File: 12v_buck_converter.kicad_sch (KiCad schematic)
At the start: 23 parts, among them IC1 TPS56A37RPAR, Q4 BUK9K52-60RAX

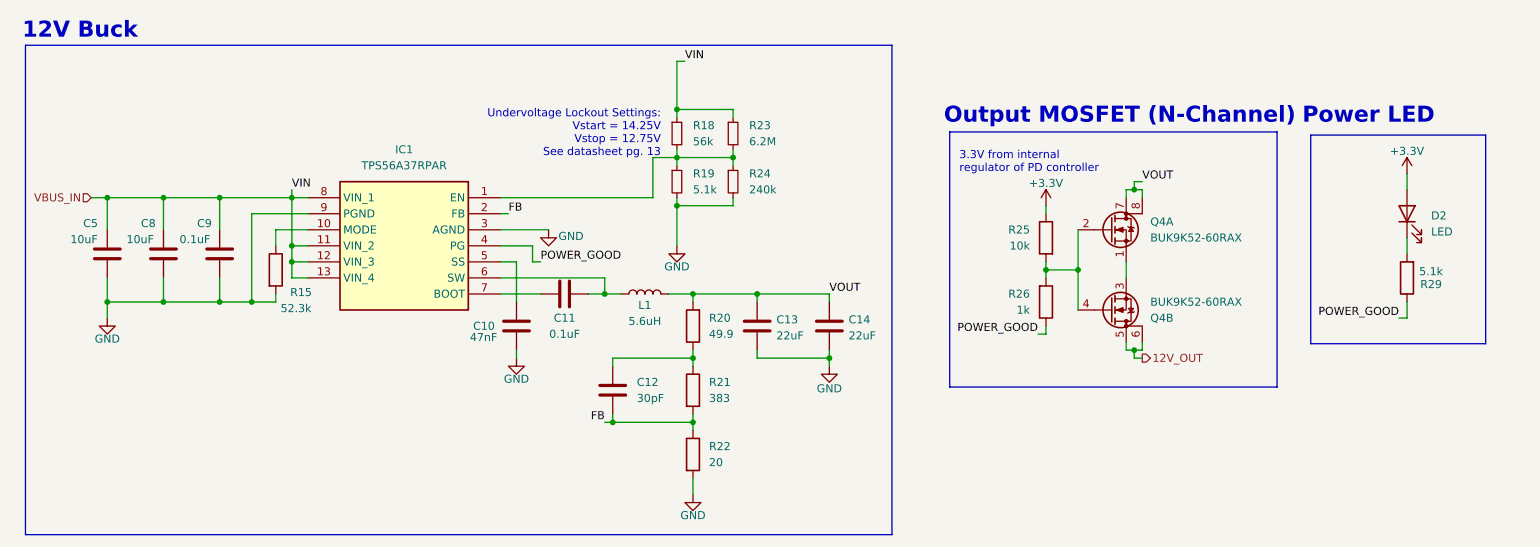
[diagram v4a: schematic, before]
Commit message: updated with some new footprints (have yet to finish footprint assignment; also need to switch out inductor for 5V buck)
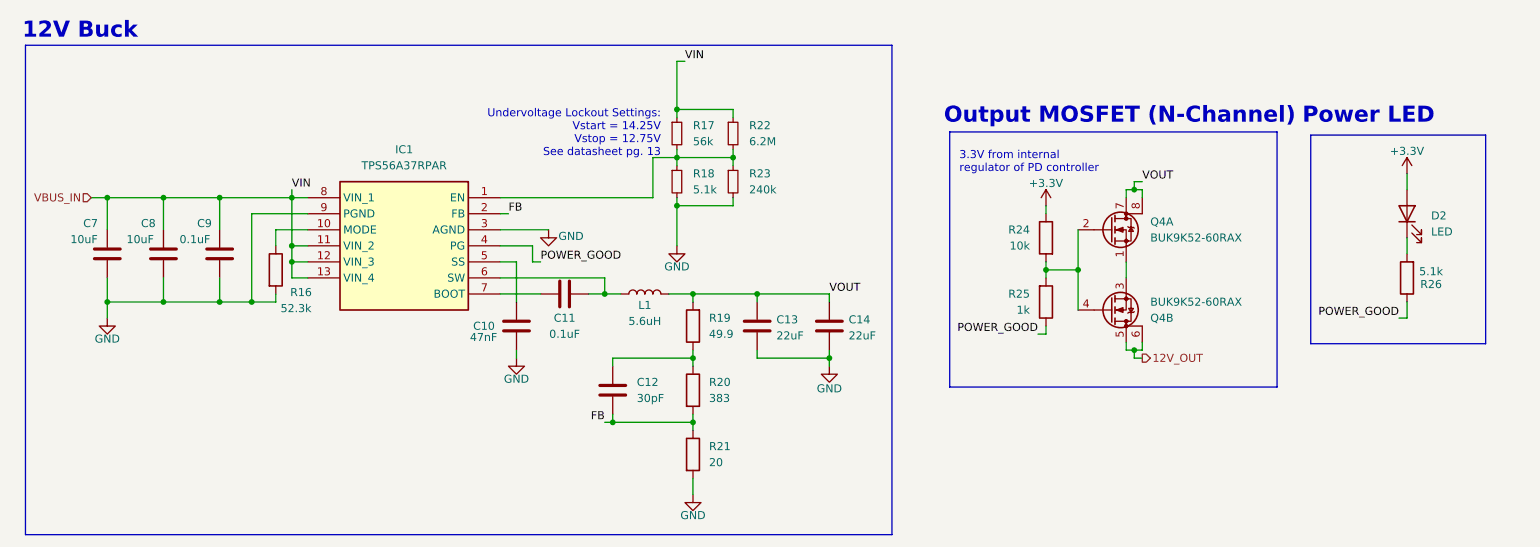
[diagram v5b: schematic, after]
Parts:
- C10, C11, C12, C13, C14, C8, C9: footprint (none) -> Capacitor_SMD:C_0805_2012Metric
- C7: renamed from C5; footprint (none) -> Capacitor_SMD:C_0805_2012Metric
- IC1: footprint TPS56A37RPAR -> UTSVT_Power:TPS56A37RPAR
- L1: footprint (none) -> UTSVT_Passive:INDPM135125X640N; Mouser Part Number (none) -> SRP1265A-5R6M
- R16: renamed from R15; footprint (none) -> Resistor_SMD:R_0805_2012Metric
- R17: renamed from R18; footprint (none) -> Resistor_SMD:R_0805_2012Metric
- R18: renamed from R19; footprint (none) -> Resistor_SMD:R_0805_2012Metric
- R19: renamed from R20; footprint (none) -> Resistor_SMD:R_0805_2012Metric
- R20: renamed from R21; footprint (none) -> Resistor_SMD:R_0805_2012Metric
- R21: renamed from R22; footprint (none) -> Resistor_SMD:R_0805_2012Metric
- R22: renamed from R23; footprint (none) -> Resistor_SMD:R_0805_2012Metric
- R23: renamed from R24; footprint (none) -> Resistor_SMD:R_0805_2012Metric
- R24: renamed from R25; footprint (none) -> Resistor_SMD:R_0805_2012Metric
- R25: renamed from R26; footprint (none) -> Resistor_SMD:R_0805_2012Metric
- R26: renamed from R29; footprint (none) -> Resistor_SMD:R_0805_2012Metric
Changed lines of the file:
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@@
 			)
 		)
-		(property "Footprint" ""
+		(property "Footprint" "Capacitor_SMD:C_0805_2012Metric"
 			(at 54.3052 99.06 0)
 			(effects
@@
 		(on_board yes)
 		(dnp no)
-		(property "Reference" "C5"
+		(property "Reference" "C7"
 			(at 40.64 90.424 0)
 			(effects
@@
 			)
 		)
-		(property "Footprint" ""
+		(property "Footprint" "Capacitor_SMD:C_0805_2012Metric"
 			(at 45.4152 99.06 0)
 			(effects
@@
 			(project "USBCPowerPCB"
 				(path "/f58400c5-df4b-4929-8d2b-33c0fe23fcd9/01d27e83-9627-42d8-8cf9-628e44513f14"
-					(reference "C5")
+					(reference "C7")
 					(unit 1)
 				)
@@
 			)
 		)
-		(property "Footprint" ""
+		(property "Footprint" "Capacitor_SMD:C_0805_2012Metric"
 			(at 159.7152 110.49 0)
 			(effects
@@
 		(dnp no)
 		(fields_autoplaced yes)
-		(property "Reference" "R25"
+		(property "Reference" "R24"
 			(at 190.5 91.4399 0)
 			(effects
@@
 			)
 		)
-		(property "Footprint" ""
+		(property "Footprint" "Resistor_SMD:R_0805_2012Metric"
 			(at 194.818 92.71 90)
 			(effects
@@
 			(project "USBCPowerPCB"
 				(path "/f58400c5-df4b-4929-8d2b-33c0fe23fcd9/01d27e83-9627-42d8-8cf9-628e44513f14"
-					(reference "R25")
+					(reference "R24")
 					(unit 1)
 				)
@@
 		(on_board yes)
 		(dnp no)
-		(property "Reference" "#PWR023"
+		(property "Reference" "#PWR025"
 			(at 114.3 97.79 0)
 			(effects
@@
 			(project "USBCPowerPCB"
 				(path "/f58400c5-df4b-4929-8d2b-33c0fe23fcd9/01d27e83-9627-42d8-8cf9-628e44513f14"
-					(reference "#PWR023")
+					(reference "#PWR025")
 					(unit 1)
 				)
@@
 			)
 		)
-		(property "Footprint" ""
+		(property "Footprint" "Capacitor_SMD:C_0805_2012Metric"
 			(at 110.1852 110.49 0)
 			(effects
@@
 		(dnp no)
 		(fields_autoplaced yes)
-		(property "Reference" "R20"
+		(property "Reference" "R19"
 			(at 139.7 105.4099 0)
 			(effects
@@
 			)
 		)
-		(property "Footprint" ""
+		(property "Footprint" "Resistor_SMD:R_0805_2012Metric"
 			(at 138.938 106.68 90)
 			(effects
@@
 			(project "USBCPowerPCB"
 				(path "/f58400c5-df4b-4929-8d2b-33c0fe23fcd9/01d27e83-9627-42d8-8cf9-628e44513f14"
-					(reference "R20")
+					(reference "R19")
 					(unit 1)
 				)
@@
 			)
 		)
-		(property "Footprint" ""
+		(property "Footprint" "Capacitor_SMD:C_0805_2012Metric"
 			(at 63.1952 99.06 0)
 			(effects
@@
 		(on_board yes)
 		(dnp no)
-		(property "Reference" "#PWR026"
+		(property "Reference" "#PWR028"
 			(at 158.75 119.38 0)
 			(effects
@@
 			(project "USBCPowerPCB"
 				(path "/f58400c5-df4b-4929-8d2b-33c0fe23fcd9/01d27e83-9627-42d8-8cf9-628e44513f14"
-					(reference "#PWR026")
+					(reference "#PWR028")
 					(unit 1)
 				)
@@
 		(dnp no)
 		(fields_autoplaced yes)
-		(property "Reference" "R18"
+		(property "Reference" "R17"
 			(at 137.16 74.9299 0)
 			(effects
@@
 			)
 		)
-		(property "Footprint" ""
+		(property "Footprint" "Resistor_SMD:R_0805_2012Metric"
 			(at 134.62 76.2 0)
 			(effects
@@
 			(project "USBCPowerPCB"
 				(path "/f58400c5-df4b-4929-8d2b-33c0fe23fcd9/01d27e83-9627-42d8-8cf9-628e44513f14"
-					(reference "R18")
+					(reference "R17")
 					(unit 1)
 				)
@@
 		(on_board yes)
 		(dnp no)
-		(property "Reference" "R15"
+		(property "Reference" "R16"
 			(at 73.406 101.346 0)
 			(effects
@@
 			)
 		)
-		(property "Footprint" ""
+		(property "Footprint" "Resistor_SMD:R_0805_2012Metric"
 			(at 69.342 97.79 90)
 			(effects
@@
 			(project "USBCPowerPCB"
 				(path "/f58400c5-df4b-4929-8d2b-33c0fe23fcd9/01d27e83-9627-42d8-8cf9-628e44513f14"
-					(reference "R15")
+					(reference "R16")
 					(unit 1)
 				)
@@
 		(dnp no)
 		(fields_autoplaced yes)
-		(property "Reference" "R19"
+		(property "Reference" "R18"
 			(at 137.16 82.5499 0)
 			(effects
@@
 			)
 		)
-		(property "Footprint" ""
+		(property "Footprint" "Resistor_SMD:R_0805_2012Metric"
 			(at 134.62 83.82 0)
 			(effects
@@
 			(project "USBCPowerPCB"
 				(path "/f58400c5-df4b-4929-8d2b-33c0fe23fcd9/01d27e83-9627-42d8-8cf9-628e44513f14"
-					(reference "R19")
+					(reference "R18")
 					(unit 1)
 				)
@@
 		(on_board yes)
 		(dnp no)
-		(property "Reference" "#PWR022"
+		(property "Reference" "#PWR024"
 			(at 109.22 118.11 0)
 			(effects
@@
 			(project "USBCPowerPCB"
 				(path "/f58400c5-df4b-4929-8d2b-33c0fe23fcd9/01d27e83-9627-42d8-8cf9-628e44513f14"
-					(reference "#PWR022")
+					(reference "#PWR024")
 					(unit 1)
 				)
@@
 			)
 		)
-		(property "Footprint" ""
+		(property "Footprint" "Capacitor_SMD:C_0805_2012Metric"
 			(at 120.65 100.6348 0)
 			(effects
@@
 			)
 		)
-		(property "Footprint" ""
+		(property "Footprint" "UTSVT_Passive:INDPM135125X640N"
 			(at 129.54 101.6 0)
 			(effects
@@
 			)
 		)
-		(property "Datasheet" "~"
+		(property "Datasheet" "https://www.mouser.com/datasheet/2/54/srp1265a-1391487.pdf"
 			(at 129.54 101.6 0)
 			(effects
@@
 			)
 		)
+		(property "Mouser Part Number" "SRP1265A-5R6M"
+			(at 129.54 101.6 0)
+			(effects
+				(font
+					(size 1.27 1.27)
+				)
+				(hide yes)
+			)
+		)
 		(pin "1"
 		)
@@
 		(on_board yes)
 		(dnp no)
-		(property "Reference" "#PWR025"
+		(property "Reference" "#PWR027"
 			(at 137.16 139.7 0)
 			(effects
@@
 			(project "USBCPowerPCB"
 				(path "/f58400c5-df4b-4929-8d2b-33c0fe23fcd9/01d27e83-9627-42d8-8cf9-628e44513f14"
-					(reference "#PWR025")
+					(reference "#PWR027")
 					(unit 1)
 				)
@@
 		(on_board yes)
 		(dnp no)
-		(property "Reference" "R26"
+		(property "Reference" "R25"
 			(at 190.5 101.5999 0)
 			(effects
@@
 			)
 		)
-		(property "Footprint" ""
+		(property "Footprint" "Resistor_SMD:R_0805_2012Metric"
 			(at 191.262 102.87 90)
 			(effects
@@
 			(project "USBCPowerPCB"
 				(path "/f58400c5-df4b-4929-8d2b-33c0fe23fcd9/01d27e83-9627-42d8-8cf9-628e44513f14"
-					(reference "R26")
+					(reference "R25")
 					(unit 1)
 				)
@@
 		(on_board yes)
 		(dnp no)
-		(property "Reference" "#PWR024"
+		(property "Reference" "#PWR026"
 			(at 134.62 100.33 0)
 			(effects
@@
 			(project "USBCPowerPCB"
 				(path "/f58400c5-df4b-4929-8d2b-33c0fe23fcd9/01d27e83-9627-42d8-8cf9-628e44513f14"
-					(reference "#PWR024")
+					(reference "#PWR026")
 					(unit 1)
 				)
@@
 		(on_board yes)
 		(dnp no)
-		(property "Reference" "R29"
+		(property "Reference" "R26"
 			(at 254 100.076 0)
 			(effects
@@
 			)
 		)
-		(property "Footprint" ""
+		(property "Footprint" "Resistor_SMD:R_0805_2012Metric"
 			(at 251.968 99.06 90)
 			(effects
@@
 			(project "USBCPowerPCB"
 				(path "/f58400c5-df4b-4929-8d2b-33c0fe23fcd9/01d27e83-9627-42d8-8cf9-628e44513f14"
-					(reference "R29")
+					(reference "R26")
 					(unit 1)
 				)
@@
 		(on_board yes)
 		(dnp no)
-		(property "Reference" "#PWR021"
+		(property "Reference" "#PWR023"
 			(at 44.45 111.76 0)
 			(effects
@@
 			(project "USBCPowerPCB"
 				(path "/f58400c5-df4b-4929-8d2b-33c0fe23fcd9/01d27e83-9627-42d8-8cf9-628e44513f14"
-					(reference "#PWR021")
+					(reference "#PWR023")
 					(unit 1)
 				)
@@
 		(dnp no)
 		(fields_autoplaced yes)
-		(property "Reference" "R23"
+		(property "Reference" "R22"
 			(at 146.05 74.9299 0)
 			(effects
@@
 			)
 		)
-		(property "Footprint" ""
+		(property "Footprint" "Resistor_SMD:R_0805_2012Metric"
 			(at 143.51 76.2 0)
 			(effects
@@
 			(project "USBCPowerPCB"
 				(path "/f58400c5-df4b-4929-8d2b-33c0fe23fcd9/01d27e83-9627-42d8-8cf9-628e44513f14"
-					(reference "R23")
+					(reference "R22")
 					(unit 1)
 				)
@@
 			)
 		)
-		(property "Footprint" "TPS56A37RPAR"
+		(property "Footprint" "UTSVT_Power:TPS56A37RPAR"
 			(at 80.01 181.28 0)
 			(effects
@@
 		(dnp no)
 		(fields_autoplaced yes)
-		(property "Reference" "R24"
+		(property "Reference" "R23"
 			(at 146.05 82.5499 0)
 			(effects
@@
 			)
 		)
-		(property "Footprint" ""
+		(property "Footprint" "Resistor_SMD:R_0805_2012Metric"
 			(at 143.51 83.82 0)
 			(effects
@@
 			(project "USBCPowerPCB"
 				(path "/f58400c5-df4b-4929-8d2b-33c0fe23fcd9/01d27e83-9627-42d8-8cf9-628e44513f14"
-					(reference "R24")
+					(reference "R23")
 					(unit 1)
 				)
@@
 		(on_board yes)
 		(dnp no)
-		(property "Reference" "#PWR033"
+		(property "Reference" "#PWR030"
 			(at 250.19 86.36 0)
 			(effects
@@
 			(project "USBCPowerPCB"
 				(path "/f58400c5-df4b-4929-8d2b-33c0fe23fcd9/01d27e83-9627-42d8-8cf9-628e44513f14"
-					(reference "#PWR033")
+					(reference "#PWR030")
 					(unit 1)
 				)
@@
 		(dnp no)
 		(fields_autoplaced yes)
-		(property "Reference" "R22"
+		(property "Reference" "R21"
 			(at 139.7 125.7299 0)
 			(effects
@@
 			)
 		)
-		(property "Footprint" ""
+		(property "Footprint" "Resistor_SMD:R_0805_2012Metric"
 			(at 135.382 127 90)
 			(effects
@@
 			(project "USBCPowerPCB"
 				(path "/f58400c5-df4b-4929-8d2b-33c0fe23fcd9/01d27e83-9627-42d8-8cf9-628e44513f14"
-					(reference "R22")
+					(reference "R21")
 					(unit 1)
 				)
@@
 			)
 		)
-		(property "Footprint" ""
+		(property "Footprint" "Capacitor_SMD:C_0805_2012Metric"
 			(at 148.2852 110.49 0)
 			(effects
@@
 			)
 		)
-		(property "Footprint" ""
+		(property "Footprint" "Capacitor_SMD:C_0805_2012Metric"
 			(at 125.4252 120.65 0)
 			(effects
@@
 		(dnp no)
 		(fields_autoplaced yes)
-		(property "Reference" "R21"
+		(property "Reference" "R20"
 			(at 139.7 115.5699 0)
 			(effects
@@
 			)
 		)
-		(property "Footprint" ""
+		(property "Footprint" "Resistor_SMD:R_0805_2012Metric"
 			(at 135.382 116.84 90)
 			(effects
@@
 			(project "USBCPowerPCB"
 				(path "/f58400c5-df4b-4929-8d2b-33c0fe23fcd9/01d27e83-9627-42d8-8cf9-628e44513f14"
-					(reference "R21")
+					(reference "R20")
 					(unit 1)
 				)
@@
 		(on_board yes)
 		(dnp no)
-		(property "Reference" "#PWR031"
+		(property "Reference" "#PWR029"
 			(at 193.04 91.44 0)
 			(effects
@@
 			(project "USBCPowerPCB"
 				(path "/f58400c5-df4b-4929-8d2b-33c0fe23fcd9/01d27e83-9627-42d8-8cf9-628e44513f14"
-					(reference "#PWR031")
-					(unit 1)
-				)
+					(reference "#PWR029")
+					(unit 1)
+				)

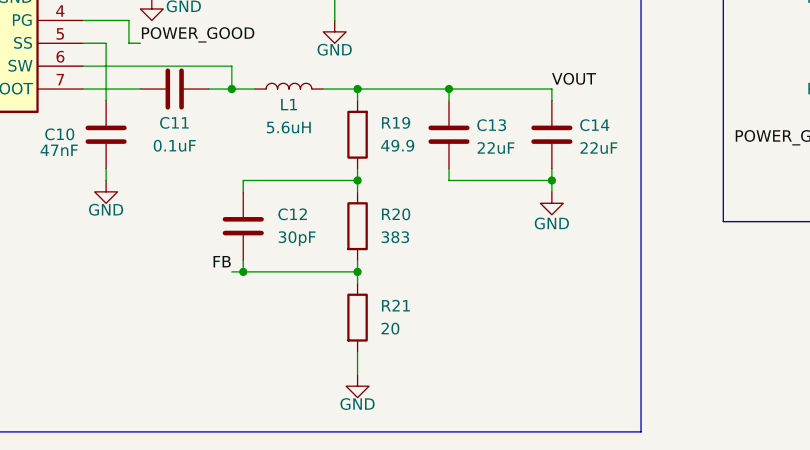
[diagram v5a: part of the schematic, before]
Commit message: changed 5v buck to TPS56A37
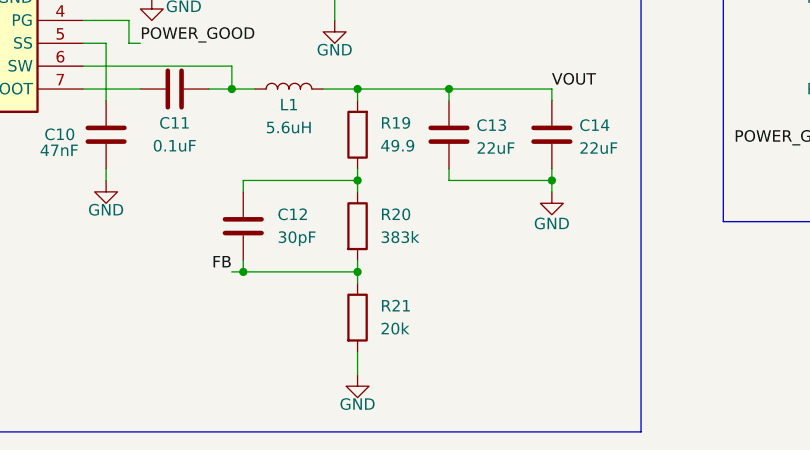
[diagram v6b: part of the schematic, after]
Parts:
- R20: value 383 -> 383k
- R21: value 20 -> 20k

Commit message: almost done w/ schematic, just need to finish footprint assignment (make sure buck converter components are correctly chosen and there aren't caps that need to be different and stuff)
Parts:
- D2: footprint (none) -> LED_SMD:LED_0805_2012Metric; Mouser Part Number (none) -> APTD2012LCGCK
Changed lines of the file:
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@@
 			)
 		)
-		(property "Datasheet" "https://www.mouser.com/datasheet/2/54/srp1265a-1391487.pdf"
+		(property "Datasheet" "https://www.mouser.com/ProductDetail/Bourns/SRP1265A-5R6M?qs=7z%252BmIopC6%2FKPWKEc%2Fy%252BgIw%3D%3D"
 			(at 129.54 101.6 0)
 			(effects
@@
 			)
 		)
-		(property "Footprint" ""
+		(property "Footprint" "LED_SMD:LED_0805_2012Metric"
 			(at 250.19 88.9 0)
 			(effects
@@
 			)
 		)
-		(property "Datasheet" "~"
+		(property "Datasheet" "https://www.mouser.com/datasheet/2/216/APTD2012LCGCK-1102037.pdf"
 			(at 250.19 88.9 0)
 			(effects
@@
 			(at 250.19 88.9 0)
 			(effects
+				(font
+					(size 1.27 1.27)
+				)
+				(hide yes)
+			)
+		)
+		(property "Mouser Part Number" "APTD2012LCGCK"
+			(at 250.19 88.9 0)
+			(effects
